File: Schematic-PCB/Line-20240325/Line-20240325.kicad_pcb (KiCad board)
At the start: 2 copper layers, 195 x 168 mm, 138 parts, among them J1 Conn_01x02_Pin, J2 Conn_01x04_Pin, J4 Conn_01x06_Pin, SW1 SW_Push, U34 ATmega2560-16A, Y1 16MHz

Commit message: らいんきばん
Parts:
- removed 330: 330, Resistor_SMD:R_0603_1608Metric
- removed D47: LED3, LED_SMD:LED_0805_2012Metric
- removed D48: LED2, LED_SMD:LED_0805_2012Metric
- removed D49: LED1, LED_SMD:LED_0805_2012Metric
- removed PWR: POWER, LED_SMD:LED_0805_2012Metric
- removed RESET: SW_Push, @2024-Line:Tactile1
- removed Y1: 16MHz, @2024TOINOT2-Line:AL4BT
- added R40: 1K, Resistor_SMD:R_0603_1608Metric, B.Cu at (-19.2, 25.2)
- C1, C10, C2, C3, C4, C5, D33, D34, D35, D36, R36, R37: moved to B.Cu
- Comp1, Comp2, Comp3, Comp4, Comp5, Comp6, Comp7, Comp8: footprint @2024TOINOT2-Line:LM339 -> @2024TOINIOT2-Line:LM339
- D1, D10, D11, D12, D13, D14, D15, D16, D17, D18, D19, D2, D20, D21, D22, D23, D24, D25, D26, D27, D28, D29, D3, D30, D31, D32, D4, D5, D6, D7, D8, D9: footprint @2024TOINOT2-Line:LED-3mm -> @2024TOINIOT2-Line:LED-3mm
- SW1: footprint @2024TOINOT2-Line:Tactile1 -> @2024TOINIOT2-Line:Tactile1; moved to B.Cu
- U1, U10, U11, U12, U13, U14, U15, U16, U17, U18, U19, U2, U20, U21, U22, U23, U24, U25, U26, U27, U28, U29, U3, U30, U31, U32, U4, U5, U6, U7, U8, U9: footprint @2024TOINOT2-Line:NJL7502L -> @2024TOINIOT2-Line:NJL7502L
- moved D34 51.0 mm to (16.2, 45.0), turned to 180 degrees
- moved D35 50.7 mm to (16.2, 47.8), turned to 180 degrees
- moved D36 50.4 mm to (16.2, 50.5), turned to 180 degrees
- moved D33 41.3 mm to (5.19, 31.2), turned to 180 degrees
- moved C1 41.1 mm to (-0.25, 30.5), turned to -90 degrees
- moved C2 39.3 mm to (-2.00, 30.5), turned to -90 degrees
- moved C3 37.5 mm to (-3.75, 30.5), turned to -90 degrees
- moved R36 36.7 mm to (11.8, 45.0), turned to 180 degrees
- moved C5 36.1 mm to (-3.75, 34.0), turned to -90 degrees
- moved C4 35.9 mm to (-5.50, 30.5), turned to -90 degrees
- moved SW1 33.9 mm to (-9.47, 26.0), turned to 90 degrees
- moved C10 32.0 mm to (-15.2, 25.2)
- moved R39 19.1 mm to (11.8, 50.5)
- moved R38 18.8 mm to (11.8, 47.8)
- moved R37 15.1 mm to (-2.00, 34.0), turned to 90 degrees
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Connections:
- Comp1 pad 1: line01 -> line04
- Comp1 pad 13: line03 -> line02
- Comp1 pad 14: line04 -> line01
- Comp1 pad 2: line02 -> line03
- Comp2 pad 1: line05 -> line08
- Comp2 pad 13: line07 -> line06
- Comp2 pad 14: line08 -> line05
- Comp2 pad 2: line06 -> line07
- Comp3 pad 1: line09 -> line12
- Comp3 pad 13: line11 -> line10
- Comp3 pad 14: line12 -> line09
- Comp3 pad 2: line10 -> line11
- Comp4 pad 1: line13 -> line16
- Comp4 pad 13: line15 -> line13
- Comp4 pad 14: line16 -> line14
- Comp4 pad 2: line14 -> line15
- Comp5 pad 1: line17 -> line20
- Comp5 pad 13: line19 -> line18
- Comp5 pad 14: line20 -> line17
- Comp5 pad 2: line18 -> line19
- Comp6 pad 1: line21 -> line23
- Comp6 pad 13: line23 -> line21
- Comp6 pad 14: line24 -> line22
- Comp6 pad 2: line22 -> line24
- Comp7 pad 1: line25 -> line28
- Comp7 pad 13: line27 -> line26
- Comp7 pad 14: line28 -> line25
- Comp7 pad 2: line26 -> line27
- Comp8 pad 1: line29 -> line31
- Comp8 pad 13: line31 -> line29
- Comp8 pad 14: line32 -> line30
- Comp8 pad 2: line30 -> line32
- U1 pad 1: Net-(Comp1-1IN+) -> Net-(Comp1-3IN+)
- U10 pad 1: Net-(Comp3-2IN+) -> Net-(Comp3-4IN+)
- U11 pad 1: Net-(Comp3-4IN+) -> Net-(Comp3-2IN+)
- U12 pad 1: Net-(Comp3-3IN+) -> Net-(Comp3-1IN+)
- U13 pad 1: Net-(Comp4-1IN+) -> Net-(Comp4-4IN+)
- U14 pad 1: Net-(Comp4-2IN+) -> Net-(Comp4-3IN+)
- U15 pad 1: Net-(Comp4-4IN+) -> Net-(Comp4-2IN+)
- U16 pad 1: Net-(Comp4-3IN+) -> Net-(Comp4-1IN+)
- U17 pad 1: Net-(Comp5-1IN+) -> Net-(Comp5-3IN+)
- U18 pad 1: Net-(Comp5-2IN+) -> Net-(Comp5-4IN+)
- U19 pad 1: Net-(Comp5-4IN+) -> Net-(Comp5-2IN+)
- U2 pad 1: Net-(Comp1-2IN+) -> Net-(Comp1-4IN+)
- U20 pad 1: Net-(Comp5-3IN+) -> Net-(Comp5-1IN+)
- U21 pad 1: Net-(Comp6-1IN+) -> Net-(Comp6-4IN+)
- U22 pad 1: Net-(Comp6-2IN+) -> Net-(Comp6-3IN+)
- U23 pad 1: Net-(Comp6-4IN+) -> Net-(Comp6-1IN+)
- U24 pad 1: Net-(Comp6-3IN+) -> Net-(Comp6-2IN+)
- U25 pad 1: Net-(Comp7-1IN+) -> Net-(Comp7-3IN+)
- U26 pad 1: Net-(Comp7-2IN+) -> Net-(Comp7-4IN+)
- U27 pad 1: Net-(Comp7-4IN+) -> Net-(Comp7-2IN+)
- U28 pad 1: Net-(Comp7-3IN+) -> Net-(Comp7-1IN+)
- U29 pad 1: Net-(Comp8-1IN+) -> Net-(Comp8-4IN+)
- U3 pad 1: Net-(Comp1-4IN+) -> Net-(Comp1-2IN+)
- U30 pad 1: Net-(Comp8-2IN+) -> Net-(Comp8-3IN+)
- U31 pad 1: Net-(Comp8-4IN+) -> Net-(Comp8-1IN+)
- U32 pad 1: Net-(Comp8-3IN+) -> Net-(Comp8-2IN+)
- U34 pad 20: line21 -> line09
- U34 pad 21: line22 -> line10
- U34 pad 22: line23 -> line11
- U34 pad 23: line24 -> line12
- U34 pad 24: unconnected-(U34-PB5/D11-Pad24) -> line13
- U34 pad 25: unconnected-(U34-PB6/D12-Pad25) -> line14
- U34 pad 26: line09 -> line15
- U34 pad 27: line10 -> line16
- U34 pad 28: line11 -> unconnected-(U34-PG3-Pad28)
- U34 pad 29: line12 -> unconnected-(U34-PG4-Pad29)
- U34 pad 47: line25 -> unconnected-(U34-PD4-Pad47)
- U34 pad 48: line26 -> unconnected-(U34-PD5-Pad48)
- U34 pad 49: line27 -> unconnected-(U34-PD6-Pad49)
- U34 pad 5: line_threshold -> Net-(U34-PE3/D5)
- U34 pad 50: line28 -> unconnected-(U34-PD7/D38-Pad50)
- U34 pad 51: line13 -> unconnected-(U34-PG0/D41-Pad51)
- U34 pad 52: line14 -> unconnected-(U34-PG1/D40-Pad52)
- U34 pad 53: line15 -> unconnected-(U34-PC0/D37-Pad53)
- U34 pad 54: line16 -> unconnected-(U34-PC1/D36-Pad54)
- U34 pad 55: line29 -> unconnected-(U34-PC2/D35-Pad55)
- U34 pad 56: line30 -> unconnected-(U34-PC3/D34-Pad56)
- U34 pad 57: line31 -> line17
- U34 pad 58: line32 -> line18
- U34 pad 59: unconnected-(U34-PC6/D31-Pad59) -> line19
- U34 pad 60: unconnected-(U34-PC7/D30-Pad60) -> line20
- U34 pad 63: line17 -> line32
- U34 pad 64: line18 -> line31
- U34 pad 65: line19 -> line30
- U34 pad 66: line20 -> line29
- U34 pad 67: unconnected-(U34-PJ4-Pad67) -> line28
- U34 pad 68: unconnected-(U34-PJ5-Pad68) -> line27
- U34 pad 69: unconnected-(U34-PJ6-Pad69) -> line26
- U34 pad 70: unconnected-(U34-PG2/D39-Pad70) -> line25
- U34 pad 71: unconnected-(U34-PA7/D29-Pad71) -> line24
- U34 pad 72: unconnected-(U34-PA6/D28-Pad72) -> line23
- U34 pad 73: unconnected-(U34-PA5/D27-Pad73) -> line22
- U34 pad 74: unconnected-(U34-PA4/D26-Pad74) -> line21
- U4 pad 1: Net-(Comp1-3IN+) -> Net-(Comp1-1IN+)
- U5 pad 1: Net-(Comp2-1IN+) -> Net-(Comp2-3IN+)
- U6 pad 1: Net-(Comp2-2IN+) -> Net-(Comp2-4IN+)
- U7 pad 1: Net-(Comp2-4IN+) -> Net-(Comp2-2IN+)
- U8 pad 1: Net-(Comp2-3IN+) -> Net-(Comp2-1IN+)
- U9 pad 1: Net-(Comp3-1IN+) -> Net-(Comp3-3IN+)
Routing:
- net +5V: track 72.2 -> 899.2 mm
- net line_threshold: track 0.00 -> 570.3 mm, vias 0 -> 7
- net line19: track 0.00 -> 170.9 mm, vias 0 -> 2
- net line20: track 0.00 -> 168.3 mm, vias 0 -> 2
- net line17: track 0.00 -> 163.6 mm, vias 0 -> 3
- net line18: track 0.00 -> 160.6 mm, vias 0 -> 2
- net line32: track 0.00 -> 148.8 mm, vias 0 -> 1
- net line31: track 0.00 -> 145.4 mm, vias 0 -> 1
- net line29: track 0.00 -> 143.9 mm, vias 0 -> 2
- net line30: track 0.00 -> 139.9 mm, vias 0 -> 2
- net line02: track 0.00 -> 132.2 mm, vias 0 -> 1
- net line01: track 0.00 -> 129.6 mm, vias 0 -> 1
- net line04: track 0.00 -> 126.7 mm, vias 0 -> 1
- net line03: track 0.00 -> 124.3 mm, vias 0 -> 2
- net Line-MD-Main=RX_5V: track 0.00 -> 116.6 mm, vias 0 -> 1
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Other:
- outline, holes or cut-outs redrawn

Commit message: ライン基板 仮完成
終わった！DRおねがい
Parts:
- moved 16MHz 1.18 mm to (-16.8, 42.8)
- moved C8 1.00 mm to (-13.2, 39.0)
- moved R35 0.98 mm to (-17.8, 41.5)
- moved C7 0.82 mm to (-20.4, 45.9)
- moved R40 0.40 mm to (-19.6, 25.2)
- moved C10 0.40 mm to (-15.6, 25.2)
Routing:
- net line_threshold: track 570.3 -> 633.4 mm, vias 7 -> 8
- net +5V: track 899.2 -> 928.3 mm, vias 0 -> 2
- net GND: track 9.67 -> 36.5 mm, vias 0 -> 9
- net Net-(Comp4-2IN+): track 17.4 -> 11.3 mm
- net Net-(U34-XTAL2): track 9.61 -> 10.7 mm
- net Net-(U34-XTAL1): track 9.63 -> 10.6 mm
- net line14: track 63.6 -> 64.4 mm
- net line17: track 163.6 -> 162.9 mm
- net line18: track 160.6 -> 159.9 mm
- net line19: track 170.9 -> 170.3 mm
- net line09: track 24.7 -> 24.1 mm
- net line10: track 27.3 -> 26.7 mm
- net line11: track 28.7 -> 28.2 mm
- net line12: track 25.1 -> 24.6 mm
- net line20: track 168.3 -> 167.8 mm
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
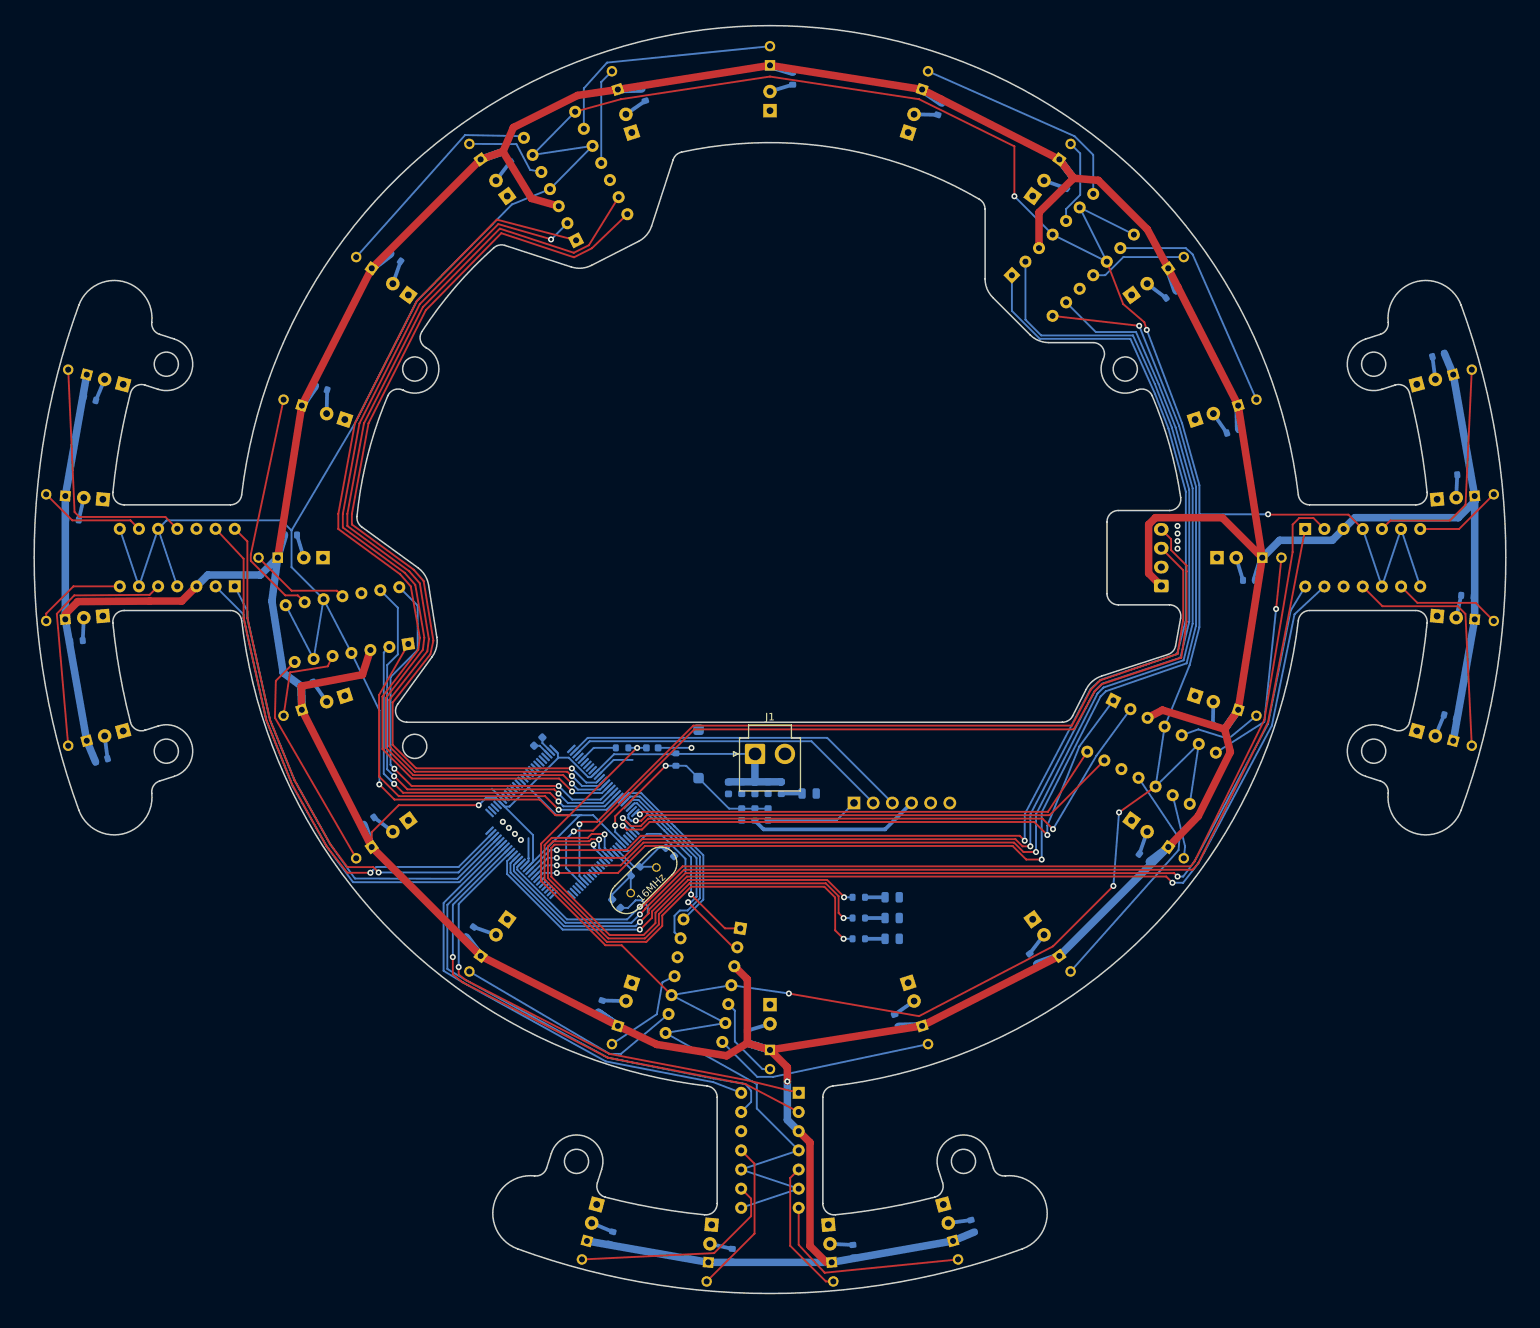
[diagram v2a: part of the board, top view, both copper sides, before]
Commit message: ラインセンサ基板 配線フィレット ほぼ完成
あとクリアランス違反解消するだけ
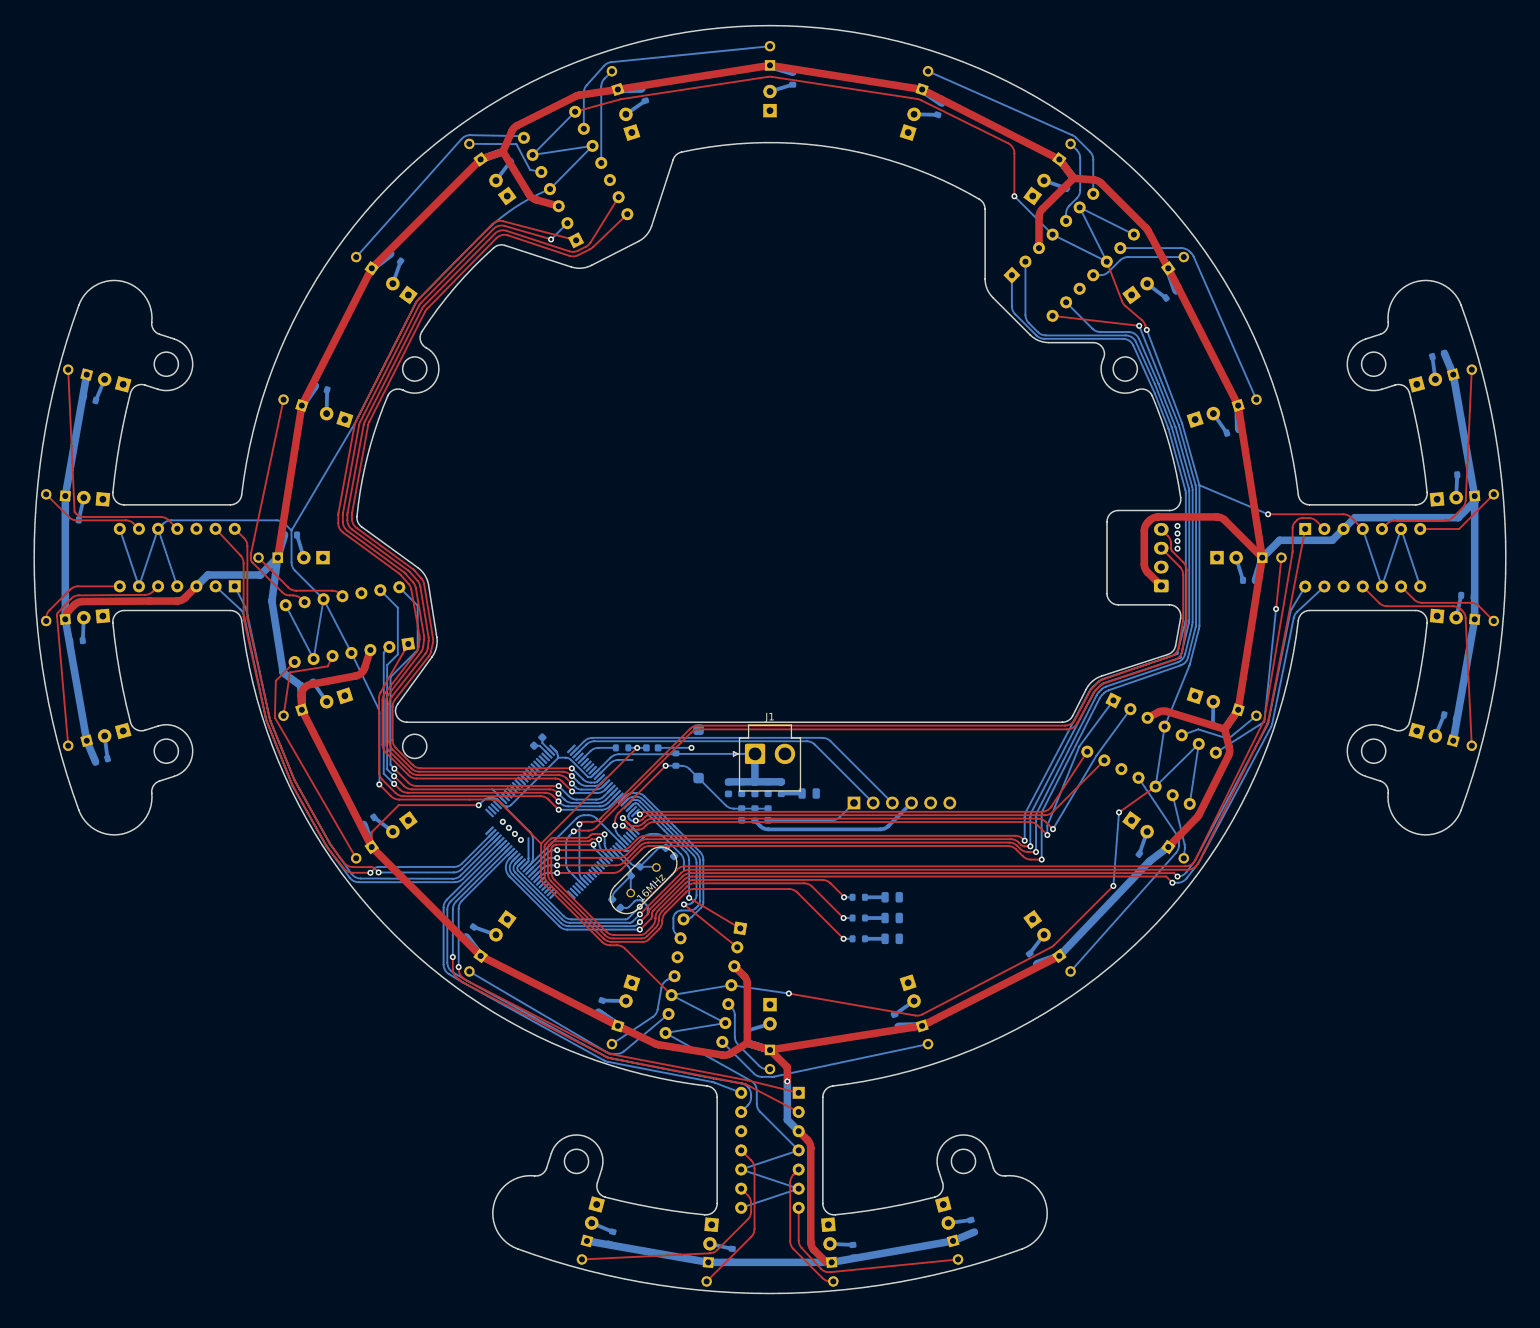
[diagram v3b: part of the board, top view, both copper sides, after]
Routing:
- net +5V: track 928.3 -> 915.7 mm
- net Net-(U34-PL0/D49): track 69.7 -> 66.2 mm
- net line_threshold: track 633.4 -> 630.7 mm
- net Net-(U34-PL1/D48): track 65.0 -> 63.0 mm
- net Line-MD-Main=RX_5V: track 116.8 -> 115.9 mm
- net line02: track 132.2 -> 131.3 mm
- net line18: track 159.9 -> 159.1 mm
- net line01: track 129.6 -> 128.8 mm
- net line03: track 124.3 -> 123.6 mm
- net line19: track 170.3 -> 169.5 mm
- net GND: track 36.5 -> 35.8 mm
- net line20: track 167.8 -> 167.1 mm
- net line04: track 126.7 -> 126.0 mm
- net Line-MD-Main=TX_5V: track 111.8 -> 111.1 mm
- net line11: track 28.2 -> 28.8 mm
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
